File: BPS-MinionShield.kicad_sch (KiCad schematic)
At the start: 79 parts, among them J1 TempConn1, J2 TempConn2, J3 Conn_01x24_Female

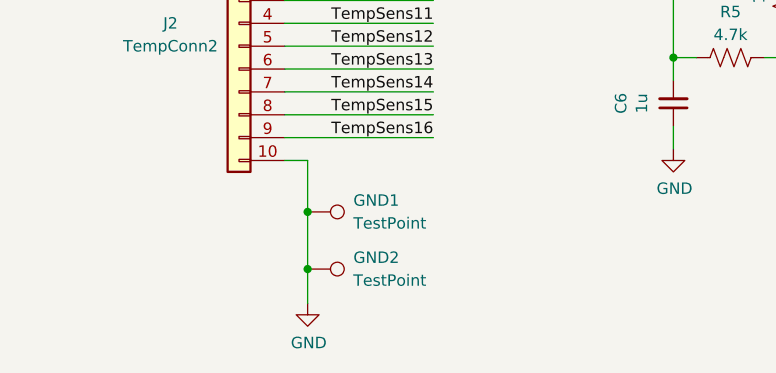
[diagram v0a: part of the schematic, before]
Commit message: keep just 1 gnd testpoint
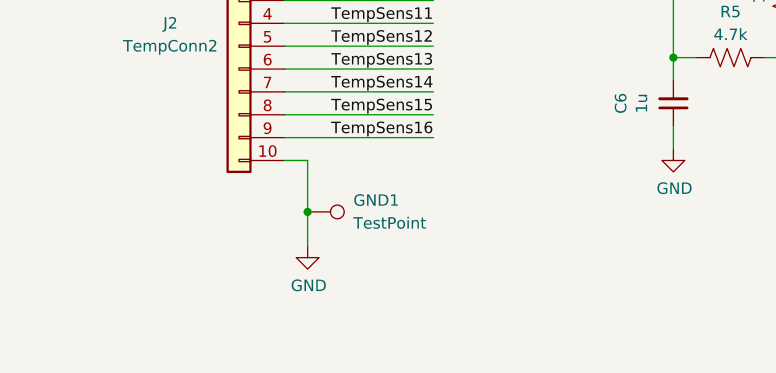
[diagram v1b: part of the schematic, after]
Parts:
- removed GND2: TestPoint, TestPoint:TestPoint_THTPad_D1.5mm_Drill0.7mm, symbol Connector:TestPoint
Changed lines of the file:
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@@
   (junction (at 196.215 150.495) (diameter 0) (color 0 0 0 0)
-  )
-  (junction (at 48.26 173.99) (diameter 0) (color 0 0 0 0)
   )
   (junction (at 48.26 167.64) (diameter 0) (color 0 0 0 0)
@@
     (stroke (width 0) (type default) (color 0 0 0 0))
   )
-  (wire (pts (xy 48.26 173.99) (xy 48.26 167.64))
+  (wire (pts (xy 48.26 167.64) (xy 48.26 171.45))
     (stroke (width 0) (type default) (color 0 0 0 0))
   )
@@
   )
   (wire (pts (xy 123.19 112.395) (xy 120.65 112.395))
-    (stroke (width 0) (type default) (color 0 0 0 0))
-  )
-  (wire (pts (xy 48.26 173.99) (xy 48.26 177.8))
     (stroke (width 0) (type default) (color 0 0 0 0))
   )
@@
     (pin "1")
   )
-  (symbol (lib_id "Connector:TestPoint") (at 48.26 173.99 270) (unit 1)
-    (in_bom yes) (on_board yes) (fields_autoplaced)
-    (property "Reference" "GND2" (id 0) (at 53.34 172.7199 90)
-      (effects (font (size 1.27 1.27)) (justify left))
-    )
-    (property "Value" "TestPoint" (id 1) (at 53.34 175.2599 90)
-      (effects (font (size 1.27 1.27)) (justify left))
-    )
-    (property "Footprint" "TestPoint:TestPoint_THTPad_D1.5mm_Drill0.7mm" (id 2) (at 48.26 179.07 0)
-      (effects (font (size 1.27 1.27)) hide)
-    )
-    (property "Datasheet" "~" (id 3) (at 48.26 179.07 0)
-      (effects (font (size 1.27 1.27)) hide)
-    )
-    (pin "1")
-  )
   (symbol (lib_id "Device:R_US") (at 196.215 104.775 180) (unit 1)
     (in_bom yes) (on_board yes)
@@
     (pin "2")
   )
-  (symbol (lib_id "power:GND") (at 48.26 177.8 0) (unit 1)
-    (in_bom yes) (on_board yes)
-    (property "Reference" "#PWR0101" (id 0) (at 48.26 184.15 0)
-      (effects (font (size 1.27 1.27)) hide)
-    )
-    (property "Value" "GND" (id 1) (at 48.387 182.1942 0))
-    (property "Footprint" "" (id 2) (at 48.26 177.8 0)
-      (effects (font (size 1.27 1.27)) hide)
-    )
-    (property "Datasheet" "" (id 3) (at 48.26 177.8 0)
+  (symbol (lib_id "power:GND") (at 48.26 171.45 0) (unit 1)
+    (in_bom yes) (on_board yes)
+    (property "Reference" "#PWR0101" (id 0) (at 48.26 177.8 0)
+      (effects (font (size 1.27 1.27)) hide)
+    )
+    (property "Value" "GND" (id 1) (at 48.387 175.8442 0))
+    (property "Footprint" "" (id 2) (at 48.26 171.45 0)
+      (effects (font (size 1.27 1.27)) hide)
+    )
+    (property "Datasheet" "" (id 3) (at 48.26 171.45 0)
       (effects (font (size 1.27 1.27)) hide)
     )
@@
       (reference "GND1") (unit 1) (value "TestPoint") (footprint "TestPoint:TestPoint_THTPad_D1.5mm_Drill0.7mm")
     )
-    (path "/5bceed01-0866-41e6-9701-c7a4fbbbfa24"
-      (reference "GND2") (unit 1) (value "TestPoint") (footprint "TestPoint:TestPoint_THTPad_D1.5mm_Drill0.7mm")
-    )
     (path "/00000000-0000-0000-0000-00005dc3a36f"

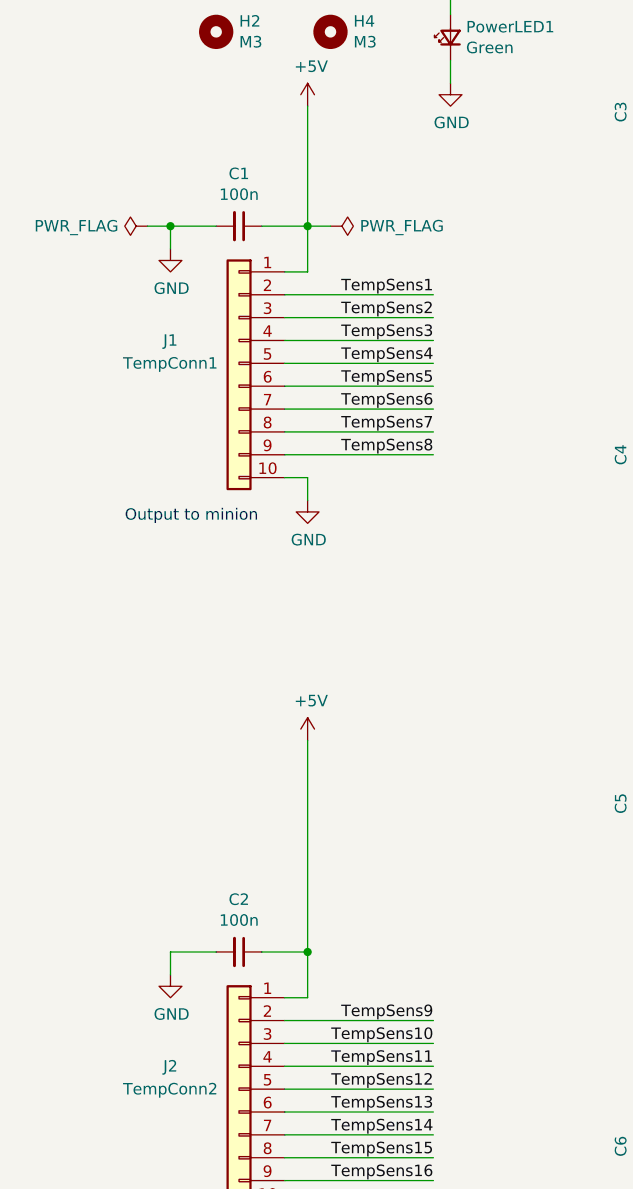
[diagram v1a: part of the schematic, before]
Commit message: move ferrite beads for more space
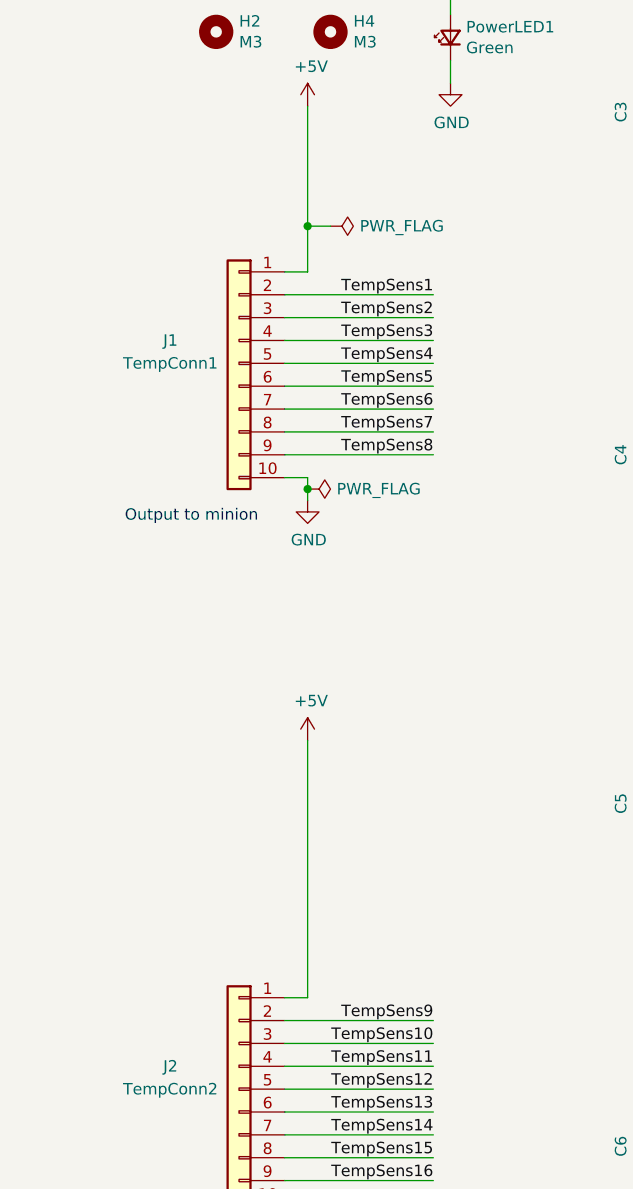
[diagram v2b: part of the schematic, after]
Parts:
- removed C1, C2: 100n, Capacitor_SMD:C_0805_2012Metric, symbol Device:C_Small
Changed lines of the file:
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@@
   (junction (at 164.465 112.395) (diameter 0) (color 0 0 0 0)
   )
+  (junction (at 48.26 82.55) (diameter 0) (color 0 0 0 0)
+  )
   (junction (at 132.715 35.56) (diameter 0) (color 0 0 0 0)
   )
@@
   (junction (at 184.15 35.56) (diameter 0) (color 0 0 0 0)
   )
-  (junction (at 48.26 133.985) (diameter 0) (color 0 0 0 0)
-  )
   (junction (at 88.9 73.66) (diameter 0) (color 0 0 0 0)
   )
@@
   )
   (junction (at 152.4 35.56) (diameter 0) (color 0 0 0 0)
-  )
-  (junction (at 33.02 53.34) (diameter 0) (color 0 0 0 0)
   )
   (junction (at 152.4 150.495) (diameter 0) (color 0 0 0 0)
@@
     (stroke (width 0) (type default) (color 0 0 0 0))
   )
-  (wire (pts (xy 33.02 133.985) (xy 33.02 136.525))
-    (stroke (width 0) (type default) (color 0 0 0 0))
-  )
-  (wire (pts (xy 33.02 53.34) (xy 33.02 55.88))
-    (stroke (width 0) (type default) (color 0 0 0 0))
-  )
   (wire (pts (xy 132.715 150.495) (xy 135.255 150.495))
     (stroke (width 0) (type default) (color 0 0 0 0))
@@
     (stroke (width 0) (type default) (color 0 0 0 0))
   )
-  (wire (pts (xy 30.48 53.34) (xy 33.02 53.34))
-    (stroke (width 0) (type default) (color 0 0 0 0))
-  )
   (wire (pts (xy 88.9 158.115) (xy 88.9 160.655))
     (stroke (width 0) (type default) (color 0 0 0 0))
@@
     (stroke (width 0) (type default) (color 0 0 0 0))
   )
-  (wire (pts (xy 48.26 133.985) (xy 48.26 139.065))
+  (wire (pts (xy 48.26 110.49) (xy 48.26 139.065))
     (stroke (width 0) (type default) (color 0 0 0 0))
   )
@@
     (stroke (width 0) (type default) (color 0 0 0 0))
   )
-  (wire (pts (xy 48.26 53.34) (xy 43.18 53.34))
-    (stroke (width 0) (type default) (color 0 0 0 0))
-  )
   (wire (pts (xy 152.4 73.66) (xy 152.4 76.2))
     (stroke (width 0) (type default) (color 0 0 0 0))
   )
-  (wire (pts (xy 48.26 83.82) (xy 48.26 81.28))
+  (wire (pts (xy 48.26 83.82) (xy 48.26 82.55))
     (stroke (width 0) (type default) (color 0 0 0 0))
   )
@@
     (stroke (width 0) (type default) (color 0 0 0 0))
   )
-  (wire (pts (xy 48.26 133.985) (xy 43.18 133.985))
-    (stroke (width 0) (type default) (color 0 0 0 0))
-  )
   (wire (pts (xy 99.06 73.66) (xy 100.965 73.66))
     (stroke (width 0) (type default) (color 0 0 0 0))
@@
     (stroke (width 0) (type default) (color 0 0 0 0))
   )
-  (wire (pts (xy 48.26 110.49) (xy 48.26 133.985))
-    (stroke (width 0) (type default) (color 0 0 0 0))
-  )
   (wire (pts (xy 203.835 35.56) (xy 207.01 35.56))
     (stroke (width 0) (type default) (color 0 0 0 0))
@@
     (stroke (width 0) (type default) (color 0 0 0 0))
   )
+  (wire (pts (xy 48.26 82.55) (xy 48.26 81.28))
+    (stroke (width 0) (type default) (color 0 0 0 0))
+  )
   (wire (pts (xy 152.4 150.495) (xy 152.4 153.035))
     (stroke (width 0) (type default) (color 0 0 0 0))
@@
     (stroke (width 0) (type default) (color 0 0 0 0))
   )
-  (wire (pts (xy 38.1 133.985) (xy 33.02 133.985))
-    (stroke (width 0) (type default) (color 0 0 0 0))
-  )
   (wire (pts (xy 164.465 35.56) (xy 167.005 35.56))
     (stroke (width 0) (type default) (color 0 0 0 0))
@@
   )
   (wire (pts (xy 88.9 35.56) (xy 88.9 38.1))
-    (stroke (width 0) (type default) (color 0 0 0 0))
-  )
-  (wire (pts (xy 38.1 53.34) (xy 33.02 53.34))
     (stroke (width 0) (type default) (color 0 0 0 0))
   )
@@
     (pin "1")
   )
-  (symbol (lib_id "power:GND") (at 33.02 136.525 0) (unit 1)
-    (in_bom yes) (on_board yes)
-    (property "Reference" "#PWR02" (id 0) (at 33.02 142.875 0)
-      (effects (font (size 1.27 1.27)) hide)
-    )
-    (property "Value" "GND" (id 1) (at 33.147 140.9192 0))
-    (property "Footprint" "" (id 2) (at 33.02 136.525 0)
-      (effects (font (size 1.27 1.27)) hide)
-    )
-    (property "Datasheet" "" (id 3) (at 33.02 136.525 0)
-      (effects (font (size 1.27 1.27)) hide)
-    )
-    (pin "1")
-  )
   (symbol (lib_id "Connector_Generic:Conn_01x10") (at 40.64 68.58 0) (mirror y) (unit 1)
     (in_bom yes) (on_board yes)
@@
     (pin "9")
   )
-  (symbol (lib_id "Device:C_Small") (at 40.64 53.34 270) (unit 1)
-    (in_bom yes) (on_board yes)
-    (property "Reference" "C1" (id 0) (at 40.64 47.5234 90))
-    (property "Value" "100n" (id 1) (at 40.64 49.8348 90))
-    (property "Footprint" "Capacitor_SMD:C_0805_2012Metric" (id 2) (at 40.64 53.34 0)
-      (effects (font (size 1.27 1.27)) hide)
-    )
-    (property "Datasheet" "https://www.mouser.com/ProductDetail/KEMET/C0805C104K5RAC?qs=r%2FVmNO8Tjq4%2F8ymSnGP6Jw%3D%3D" (id 3) (at 40.64 53.34 0)
-      (effects (font (size 1.27 1.27)) hide)
-    )
-    (pin "1")
-    (pin "2")
-  )
-  (symbol (lib_id "power:GND") (at 33.02 55.88 0) (unit 1)
-    (in_bom yes) (on_board yes)
-    (property "Reference" "#PWR01" (id 0) (at 33.02 62.23 0)
-      (effects (font (size 1.27 1.27)) hide)
-    )
-    (property "Value" "GND" (id 1) (at 33.147 60.2742 0))
-    (property "Footprint" "" (id 2) (at 33.02 55.88 0)
-      (effects (font (size 1.27 1.27)) hide)
-    )
-    (property "Datasheet" "" (id 3) (at 33.02 55.88 0)
-      (effects (font (size 1.27 1.27)) hide)
-    )
-    (pin "1")
-  )
   (symbol (lib_id "power:GND") (at 48.26 83.82 0) (unit 1)
     (in_bom yes) (on_board yes)
@@
     (pin "1")
   )
-  (symbol (lib_id "power:PWR_FLAG") (at 30.48 53.34 90) (unit 1)
-    (in_bom yes) (on_board yes)
-    (property "Reference" "#FLG01" (id 0) (at 28.575 53.34 0)
-      (effects (font (size 1.27 1.27)) hide)
-    )
-    (property "Value" "PWR_FLAG" (id 1) (at 27.2542 53.34 90)
+  (symbol (lib_id "power:PWR_FLAG") (at 48.26 82.55 270) (unit 1)
+    (in_bom yes) (on_board yes)
+    (property "Reference" "#FLG01" (id 0) (at 50.165 82.55 0)
+      (effects (font (size 1.27 1.27)) hide)
+    )
+    (property "Value" "PWR_FLAG" (id 1) (at 51.4858 82.55 90)
       (effects (font (size 1.27 1.27)) (justify left))
     )
-    (property "Footprint" "" (id 2) (at 30.48 53.34 0)
-      (effects (font (size 1.27 1.27)) hide)
-    )
-    (property "Datasheet" "~" (id 3) (at 30.48 53.34 0)
+    (property "Footprint" "" (id 2) (at 48.26 82.55 0)
+      (effects (font (size 1.27 1.27)) hide)
+    )
+    (property "Datasheet" "~" (id 3) (at 48.26 82.55 0)
       (effects (font (size 1.27 1.27)) hide)
     )
@@
     (pin "2")
   )
-  (symbol (lib_id "Device:C_Small") (at 40.64 133.985 270) (unit 1)
-    (in_bom yes) (on_board yes)
-    (property "Reference" "C2" (id 0) (at 40.64 128.1684 90))
-    (property "Value" "100n" (id 1) (at 40.64 130.4798 90))
-    (property "Footprint" "Capacitor_SMD:C_0805_2012Metric" (id 2) (at 40.64 133.985 0)
-      (effects (font (size 1.27 1.27)) hide)
-    )
-    (property "Datasheet" "https://www.mouser.com/ProductDetail/KEMET/C0805C104K5RAC?qs=r%2FVmNO8Tjq4%2F8ymSnGP6Jw%3D%3D" (id 3) (at 40.64 133.985 0)
-      (effects (font (size 1.27 1.27)) hide)
-    )
-    (pin "1")
-    (pin "2")
-  )
   (symbol (lib_id "power:GND") (at 152.4 45.72 0) (unit 1)
     (in_bom yes) (on_board yes)
@@
       (reference "#FLG02") (unit 1) (value "PWR_FLAG") (footprint "")
     )
-    (path "/00000000-0000-0000-0000-00005db6d147"
-      (reference "#PWR01") (unit 1) (value "GND") (footprint "")
-    )
-    (path "/00000000-0000-0000-0000-00005db62854"
-      (reference "#PWR02") (unit 1) (value "GND") (footprint "")
-    )
     (path "/00000000-0000-0000-0000-00005db78fe4"
       (reference "#PWR03") (unit 1) (value "+5V") (footprint "")
@@
       (reference "#PWR0101") (unit 1) (value "GND") (footprint "")
     )
-    (path "/00000000-0000-0000-0000-00005db6d140"
-      (reference "C1") (unit 1) (value "100n") (footprint "Capacitor_SMD:C_0805_2012Metric")
-    )
-    (path "/7354a4be-ec88-418b-90fe-a8546f86138b"
-      (reference "C2") (unit 1) (value "100n") (footprint "Capacitor_SMD:C_0805_2012Metric")
-    )
     (path "/0f5e7c1d-b9d8-449c-b2b3-c87304cc4238"
